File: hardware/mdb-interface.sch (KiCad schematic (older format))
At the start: 77 parts, among them IC1 ATMEGA644PA-A, J1 USB, K1 *, K2 *, P1 CONN_24, P10 CONN_1, P11 CONN_1, P12 CONN_1, P2 CONN_12V, P3 CONN_6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

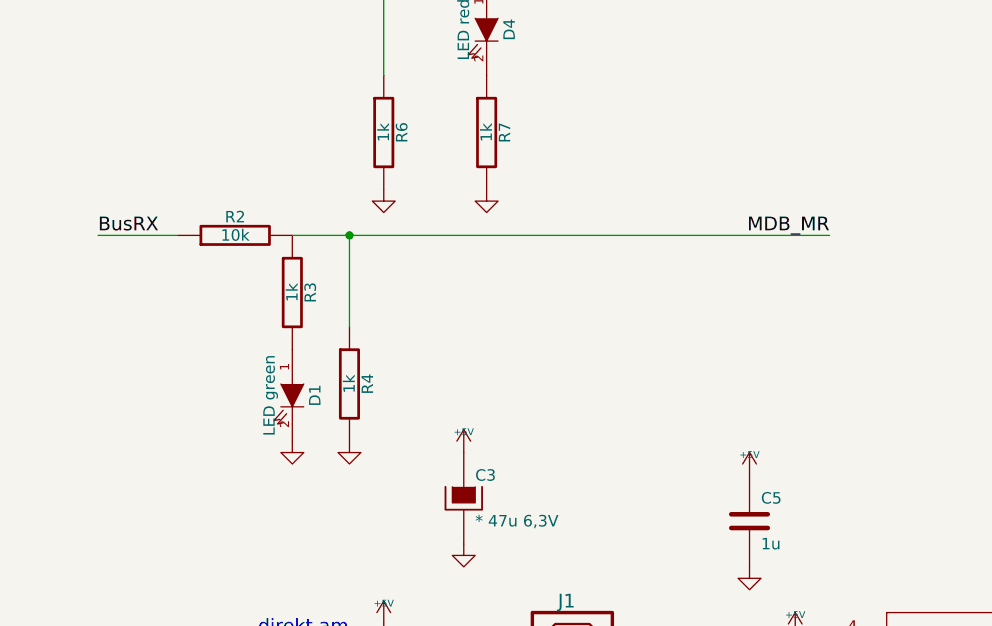
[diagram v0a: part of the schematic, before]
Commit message: MDB_MR PULL-Up statt Pull-Down. fixes #10 falls die Diode passt
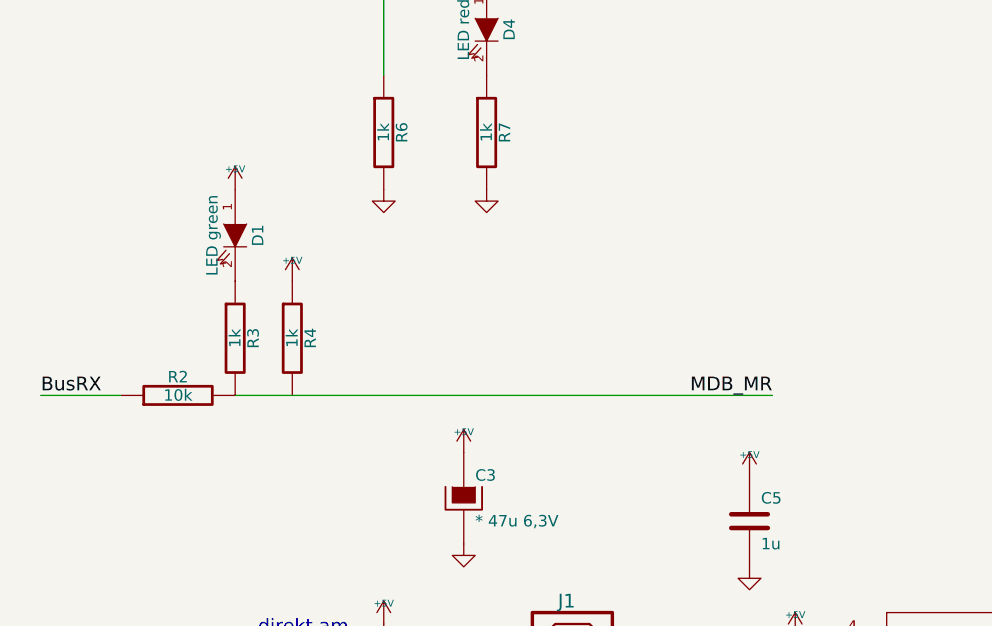
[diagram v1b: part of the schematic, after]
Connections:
- net +5V: now also D1.1 (A), R4.1
- net GND: no longer D1.2 (K), R4.2
- net MDB_MR: now also R3.2; no longer R3.1, R4.1
- new net: D1.2 (K), R3.1
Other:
- moved on the sheet: D1, R2, R3, R4

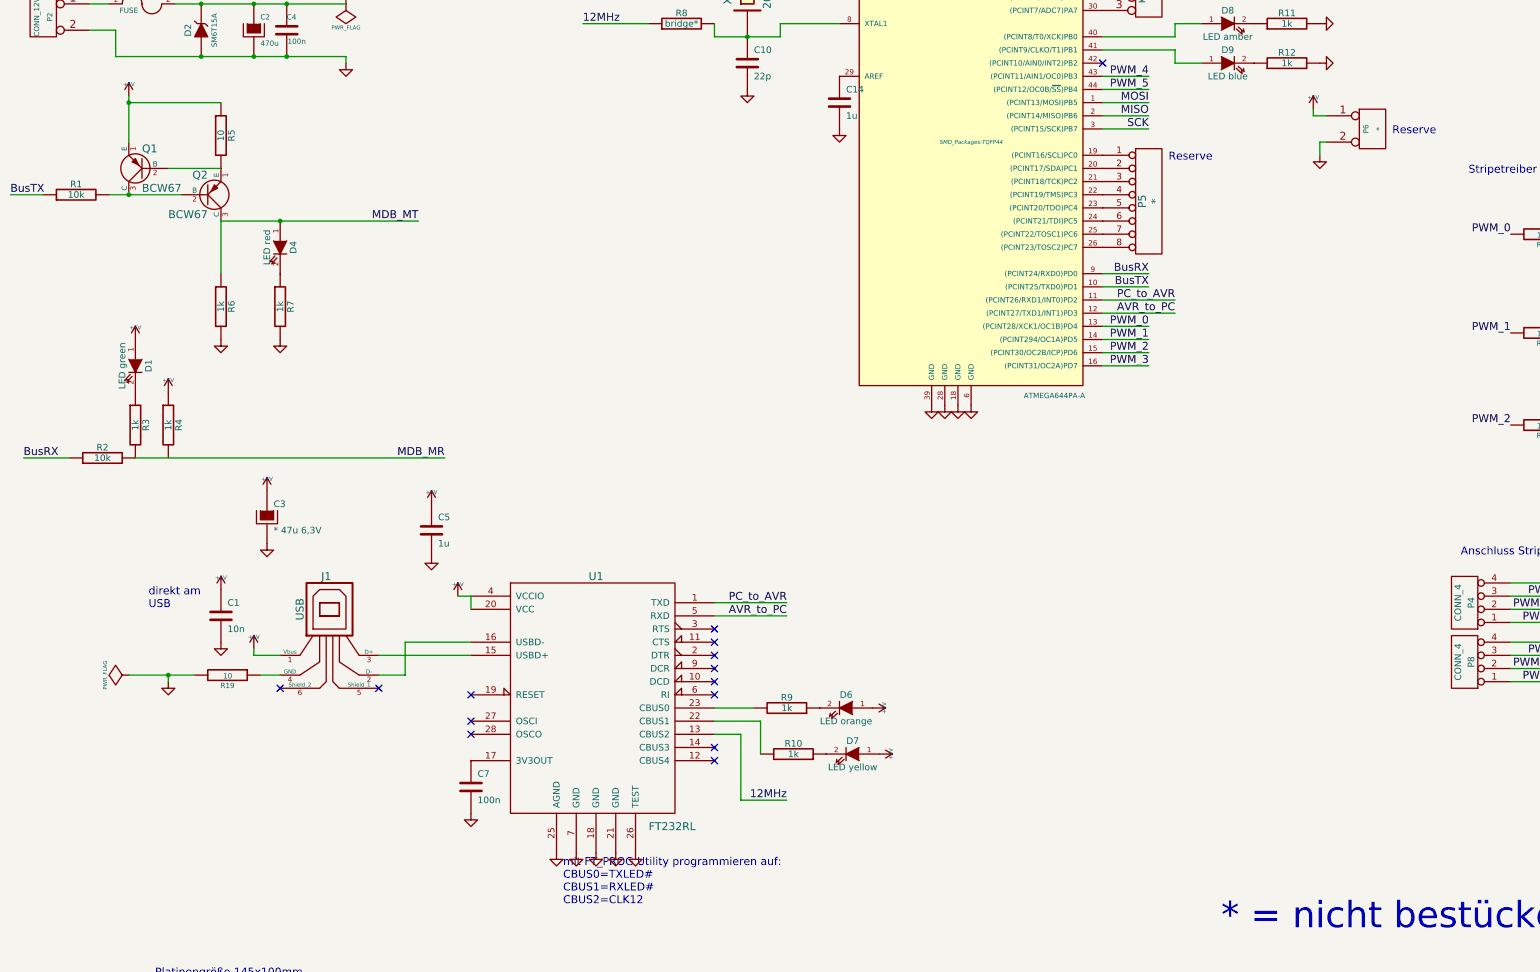
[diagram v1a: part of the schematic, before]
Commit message: lötbrücke für 5V hinzugefügt, fixes #13
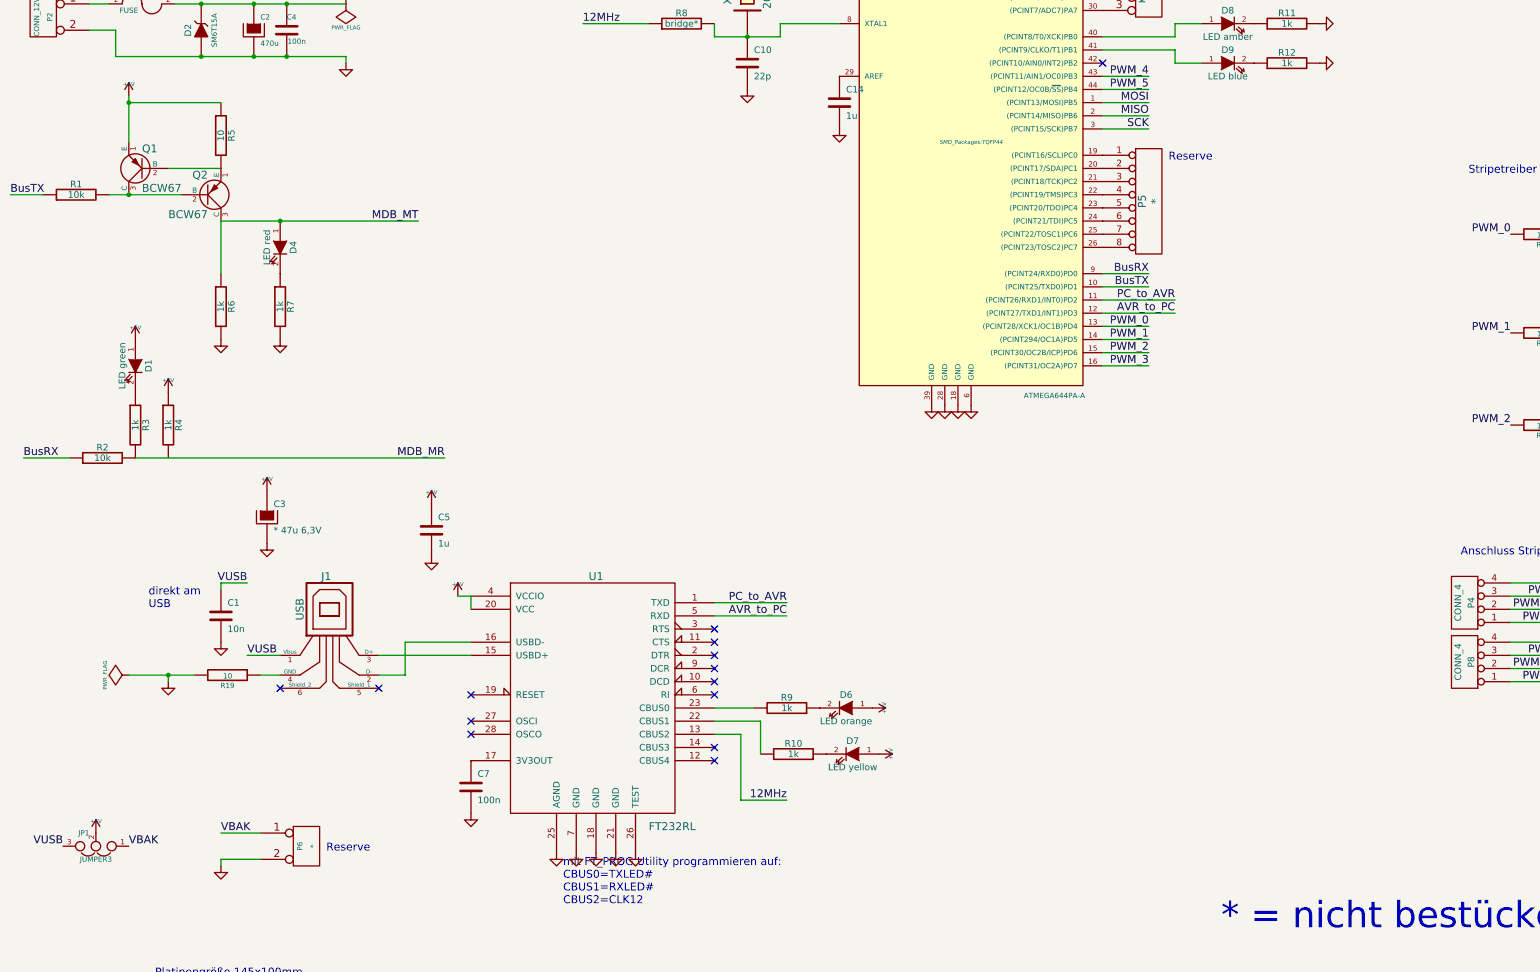
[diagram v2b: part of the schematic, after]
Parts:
- added JP1: JUMPER3, Oddities:NetTie-II_SMD, symbol JUMPER3
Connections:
- net +5V: now also JP1.2; no longer C1.1, J1.1 (Vbus), P6.1 (P1)
- new net VBAK: JP1.1, P6.1 (P1)
- new net VUSB: C1.1, J1.1 (Vbus), JP1.3
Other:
- moved on the sheet: P6

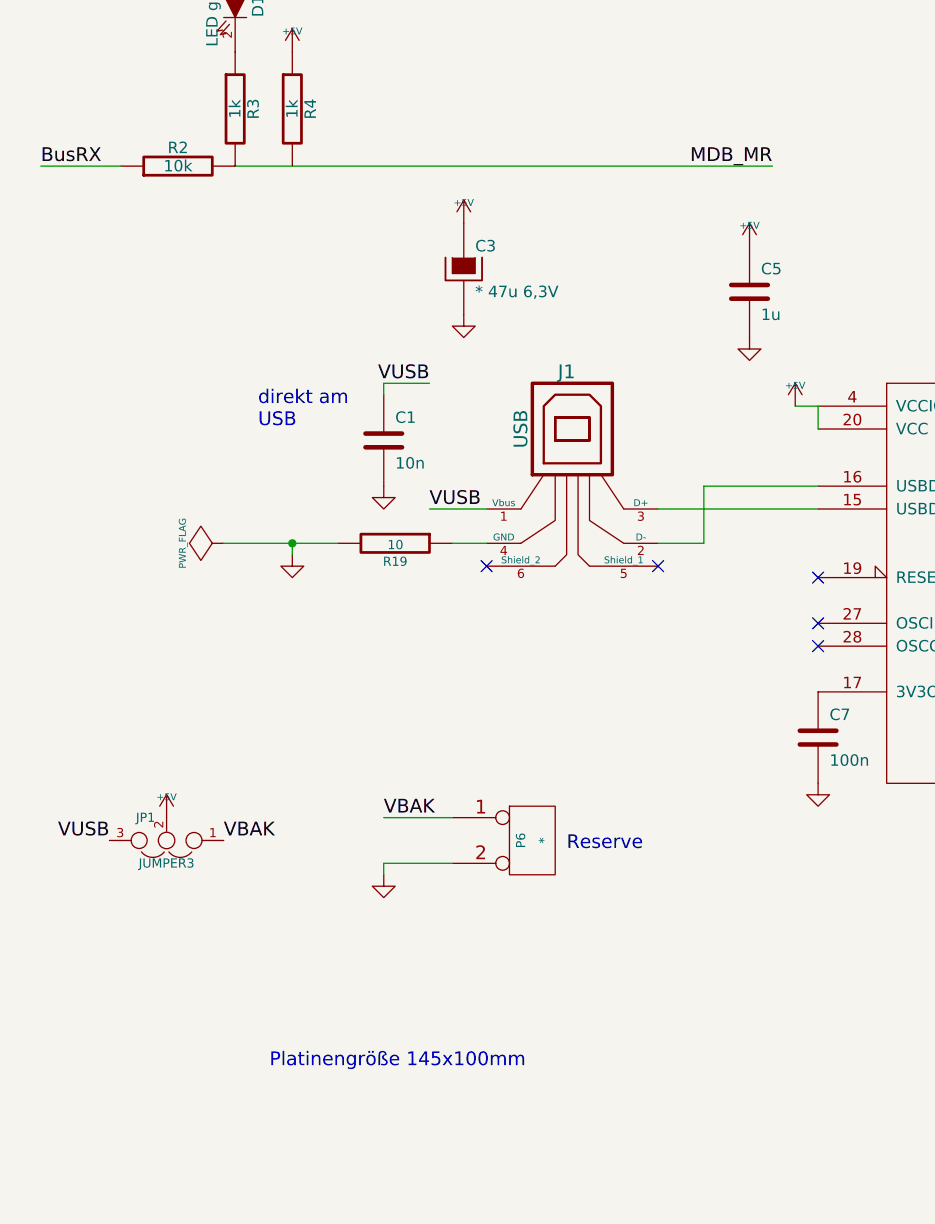
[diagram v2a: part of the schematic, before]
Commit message: extra GND Pin, fixes #12
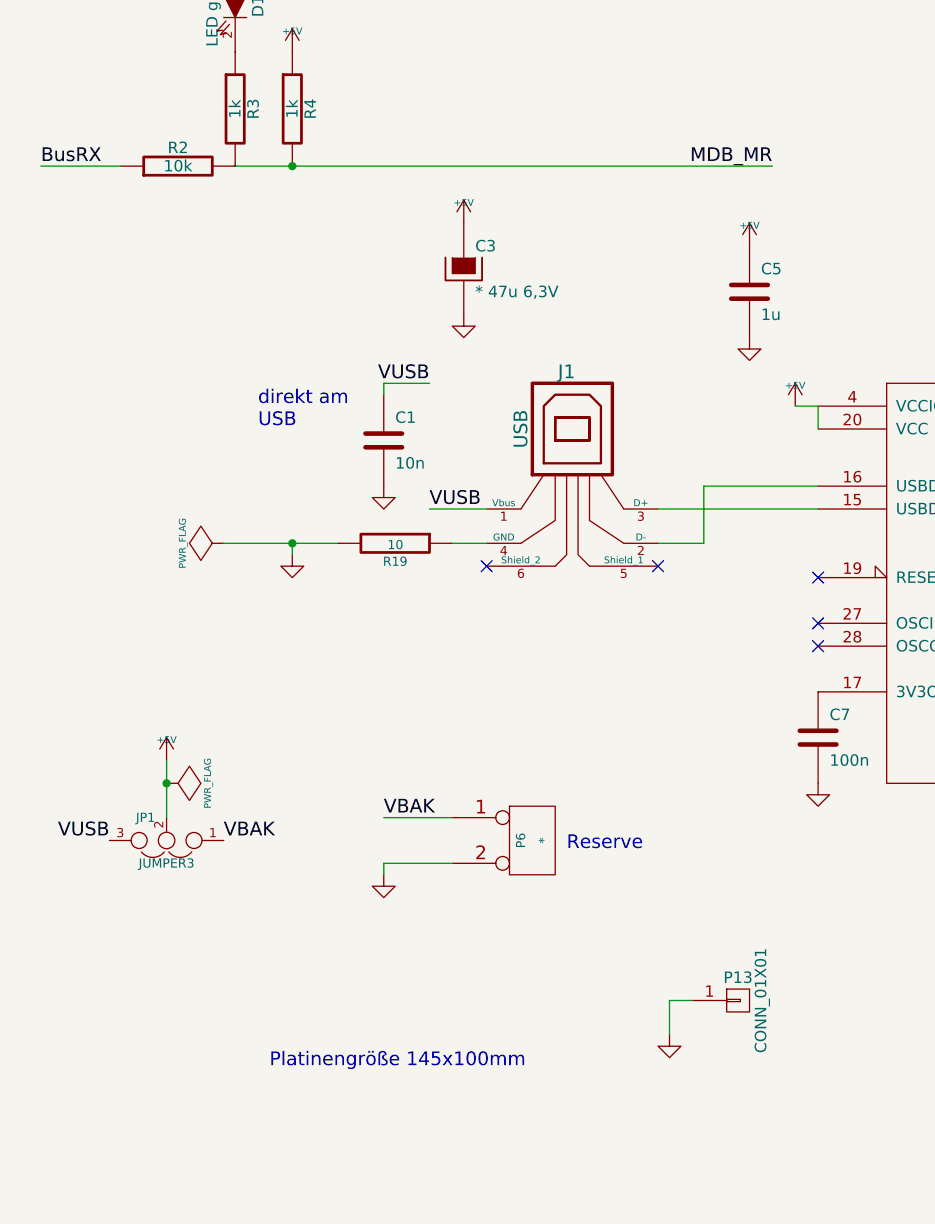
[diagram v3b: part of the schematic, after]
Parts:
- added P13: CONN_01X01, Connect:1pin, symbol CONN_01X01
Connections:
- net GND: now also P13.1 (P1)
- net MDB_MR: now also R4.2
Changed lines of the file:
@@
 L +5V #PWR058
 U 1 1 54BC0B4A
-P 1300 8900
-F 0 "#PWR058" H 1300 8990 20  0001 C CNN
-F 1 "+5V" H 1300 8990 30  0000 C CNN
-F 2 "" H 1300 8900 60  0001 C CNN
-F 3 "" H 1300 8900 60  0001 C CNN
-	1    1300 8900
+P 1300 8650
+F 0 "#PWR058" H 1300 8740 20  0001 C CNN
+F 1 "+5V" H 1300 8740 30  0000 C CNN
+F 2 "" H 1300 8650 60  0001 C CNN
+F 3 "" H 1300 8650 60  0001 C CNN
+	1    1300 8650
 	1    0    0    -1
 $EndComp
+$Comp
+L CONN_01X01 P13
+U 1 1 54BBCBCD
+P 3800 9700
+F 0 "P13" H 3800 9800 50  0000 C CNN
+F 1 "CONN_01X01" V 3900 9700 50  0000 C CNN
+F 2 "Connect:1pin" H 3800 9700 60  0001 C CNN
+F 3 "" H 3800 9700 60  0000 C CNN
+	1    3800 9700
+	1    0    0    -1
+$EndComp
+$Comp
+L GND #PWR059
+U 1 1 54BBCC51
+P 3500 9850
+F 0 "#PWR059" H 3500 9850 30  0001 C CNN
+F 1 "GND" H 3500 9780 30  0001 C CNN
+F 2 "" H 3500 9850 60  0001 C CNN
+F 3 "" H 3500 9850 60  0001 C CNN
+	1    3500 9850
+	1    0    0    -1
+$EndComp
+Wire Wire Line
+	3600 9700 3500 9700
+Wire Wire Line
+	3500 9700 3500 9850
+$Comp
+L PWR_FLAG #FLG060
+U 1 1 54BBDB76
+P 1300 8750
+F 0 "#FLG060" H 1300 8845 30  0001 C CNN
+F 1 "PWR_FLAG" H 1300 8930 30  0000 C CNN
+F 2 "" H 1300 8750 60  0001 C CNN
+F 3 "" H 1300 8750 60  0001 C CNN
+	1    1300 8750
+	0    1    1    0
+$EndComp
+Wire Wire Line
+	1300 8650 1300 8900
+Connection ~ 1300 8750
+Connection ~ 1850 6050
 $EndSCHEMATC

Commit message: added schematic symbol for PNP with swapped leads, fixes #9
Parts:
- Q1, Q2: footprint Transistors_SMD:sot23 -> (none)
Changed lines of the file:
@@
 LIBS:contrib
 LIBS:valves
+LIBS:pnp
 LIBS:mdb-interface-cache
 EELAYER 25 0
@@
 	1    0    0    -1
 $EndComp
-$Comp
-L PNP Q1
-U 1 1 531B3BC3
-P 1650 3850
-F 0 "Q1" H 1650 3700 60  0000 R CNN
-F 1 "BCW67" H 1650 4000 60  0000 R CNN
-F 2 "Transistors_SMD:sot23" H 1650 3850 60  0001 C CNN
-F 3 "" H 1650 3850 60  0001 C CNN
-	1    1650 3850
-	-1   0    0    1
-$EndComp
-$Comp
-L PNP Q2
-U 1 1 531B3BBC
-P 2150 4050
-F 0 "Q2" H 2150 3900 60  0000 R CNN
-F 1 "BCW67" H 2150 4200 60  0000 R CNN
-F 2 "Transistors_SMD:sot23" H 2150 4050 60  0001 C CNN
-F 3 "" H 2150 4050 60  0001 C CNN
-	1    2150 4050
-	1    0    0    1
-$EndComp
 Wire Wire Line
 	6950 2250 6950 2350
@@
 Connection ~ 1300 8750
 Connection ~ 1850 6050
+$Comp
+L PNP Q1
+U 1 1 54BBB005
+P 1650 3850
+F 0 "Q1" H 1650 3700 60  0000 R CNN
+F 1 "BCW67" H 1650 4000 60  0000 R CNN
+F 2 "" H 1650 3850 60  0000 C CNN
+F 3 "" H 1650 3850 60  0000 C CNN
+	1    1650 3850
+	-1   0    0    1
+$EndComp
+$Comp
+L PNP Q2
+U 1 1 54BBB1C4
+P 2150 4050
+F 0 "Q2" H 2150 3900 60  0000 R CNN
+F 1 "BCW67" H 2150 4200 60  0000 R CNN
+F 2 "" H 2150 4050 60  0000 C CNN
+F 3 "" H 2150 4050 60  0000 C CNN
+	1    2150 4050
+	1    0    0    1
+$EndComp
 $EndSCHEMATC
